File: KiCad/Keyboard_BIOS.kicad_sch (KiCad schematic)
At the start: 19 parts, among them J1 Keyboard, J2 Mouse, U4 8242KBD, U401 74F32, U5 SST39SF010A, U61 74LS06

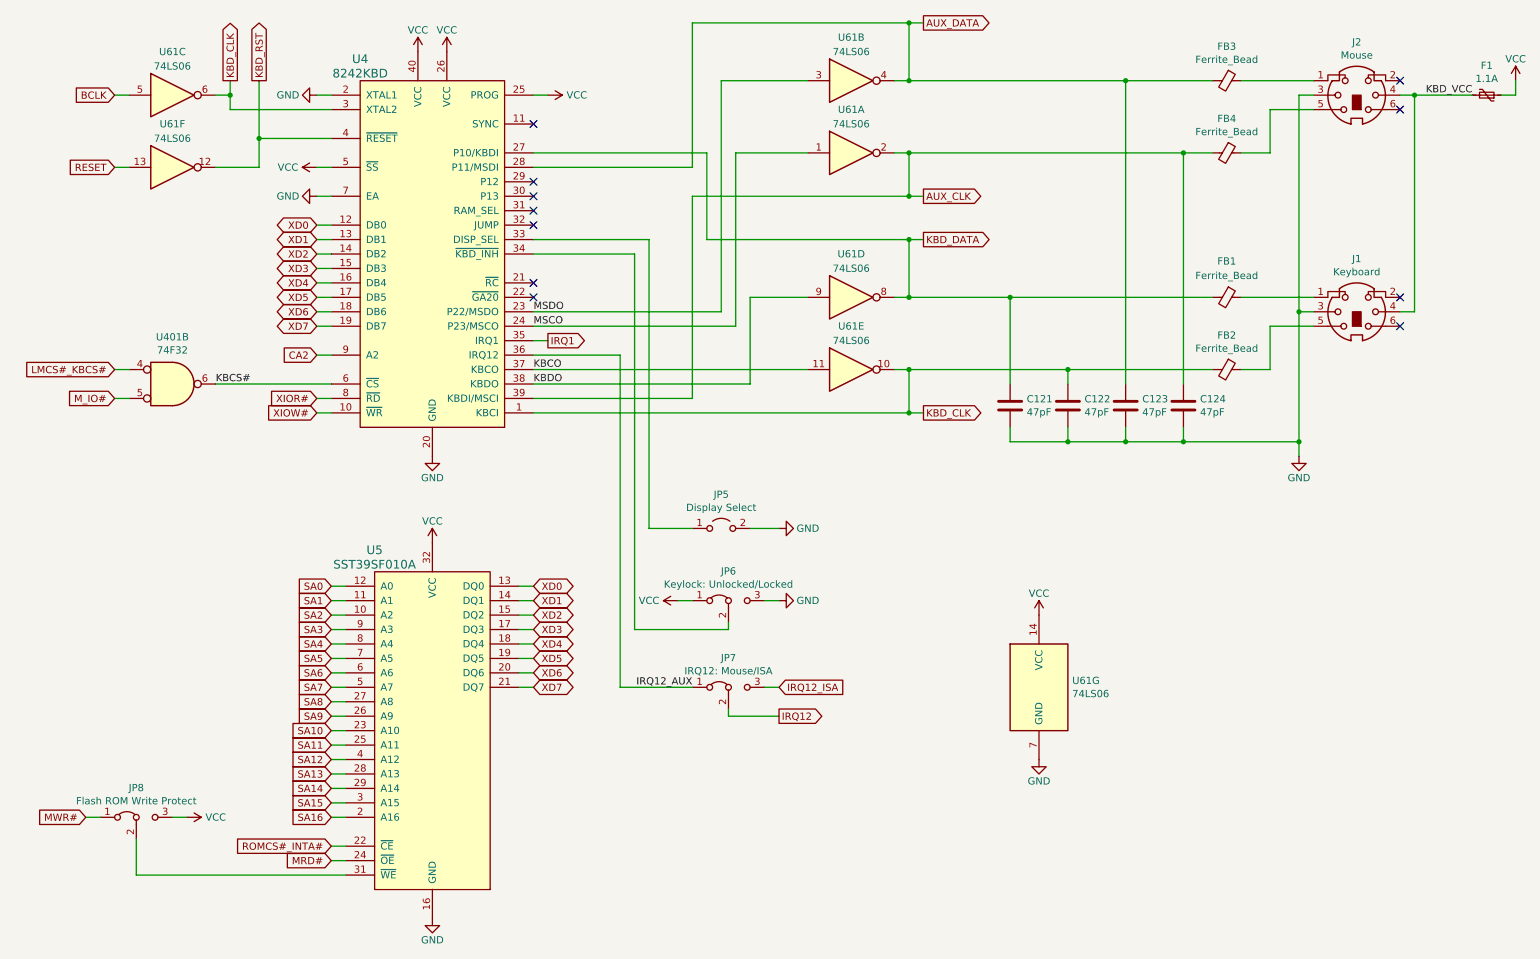
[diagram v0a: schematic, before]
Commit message: Version 0.3: Update DRAM schematic, pull-ups/pull-downs, CPU configuration jumpers
Signed-off-by: Sergey Kiselev <skiselev@gmail.com>
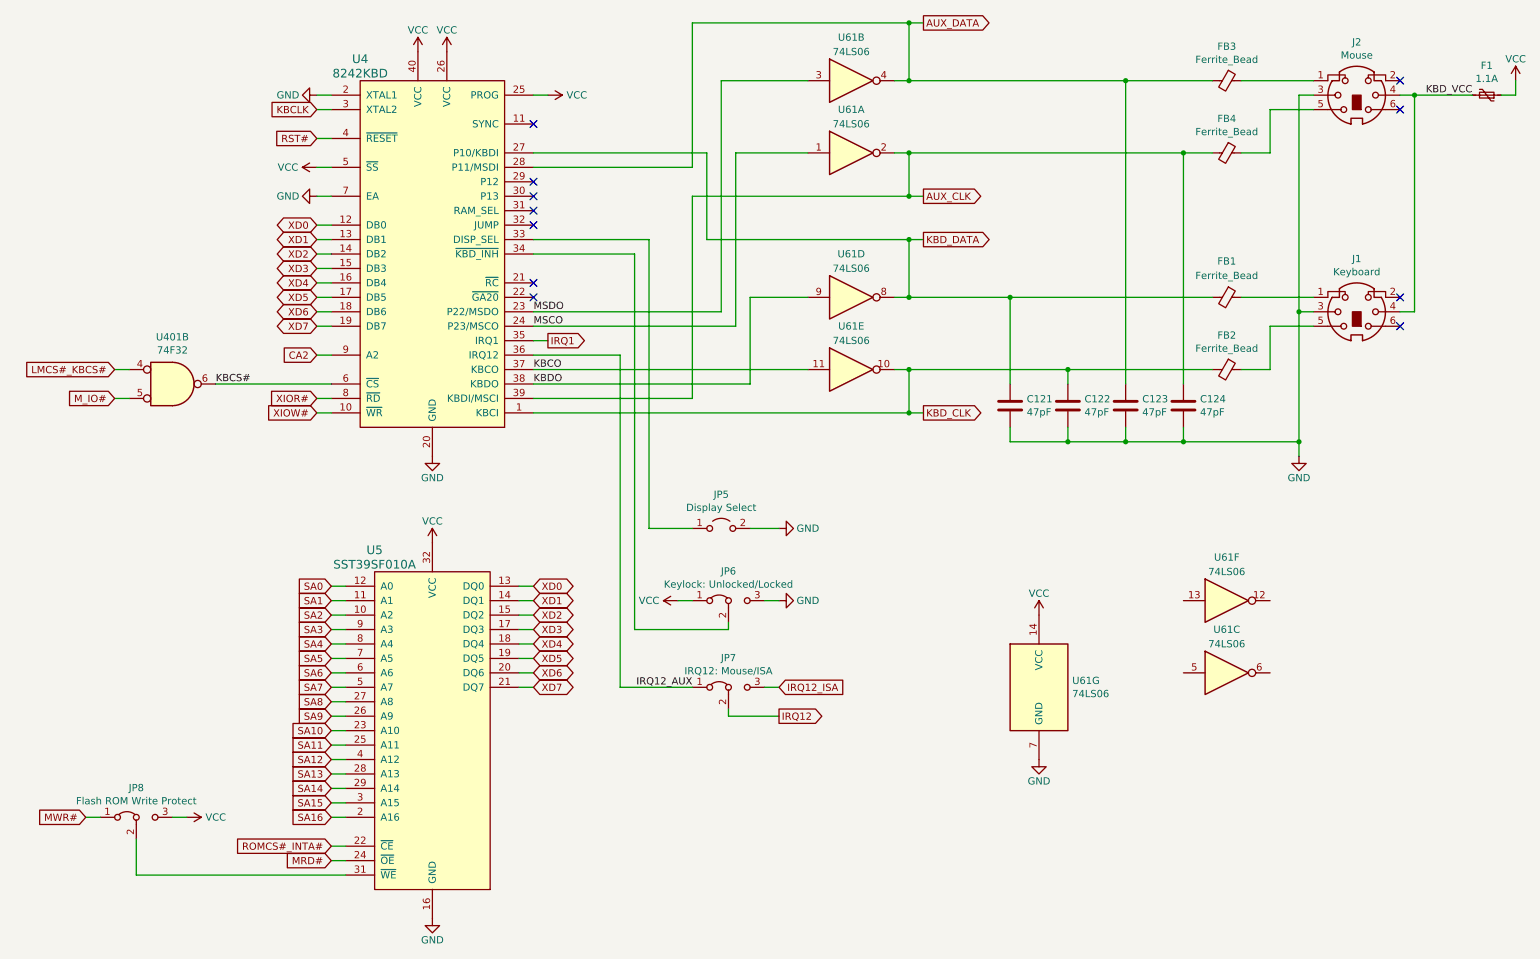
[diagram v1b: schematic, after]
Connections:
- net KBD_CLK: no longer U4.3 (XTAL2), U61.6
- net BCLK: no longer names the net of U61.5
- net KBD_RST: no longer names the net of U61.12
- net KBD_RST: no longer U4.4 (~{RESET})
- net RESET: no longer names the net of U61.13
- new net KBCLK: U4.3 (XTAL2)
- new net RST#: U4.4 (~{RESET})
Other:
- moved on the sheet: U61C, U61F
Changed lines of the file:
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@@
   (junction (at 215.9 48.26) (diameter 0) (color 0 0 0 0)
   )
-  (junction (at 48.26 38.1) (diameter 0) (color 0 0 0 0)
-  )
   (junction (at 256.54 38.1) (diameter 0) (color 0 0 0 0)
   )
@@
   )
   (junction (at 215.9 99.06) (diameter 0) (color 0 0 0 0)
-  )
-  (junction (at 53.34 45.72) (diameter 0) (color 0 0 0 0)
   )
   (junction (at 195.58 86.36) (diameter 0) (color 0 0 0 0)
@@
     (stroke (width 0) (type default) (color 0 0 0 0))
   )
-  (wire (pts (xy 48.26 38.1) (xy 48.26 40.64))
-    (stroke (width 0) (type default) (color 0 0 0 0))
-  )
   (wire (pts (xy 68.58 124.46) (xy 66.04 124.46))
     (stroke (width 0) (type default) (color 0 0 0 0))
@@
     (stroke (width 0) (type default) (color 0 0 0 0))
   )
-  (wire (pts (xy 45.72 38.1) (xy 48.26 38.1))
-    (stroke (width 0) (type default) (color 0 0 0 0))
-  )
   (wire (pts (xy 101.6 81.28) (xy 104.14 81.28))
     (stroke (width 0) (type default) (color 0 0 0 0))
@@
     (stroke (width 0) (type default) (color 0 0 0 0))
   )
-  (wire (pts (xy 53.34 45.72) (xy 53.34 35.56))
-    (stroke (width 0) (type default) (color 0 0 0 0))
-  )
   (wire (pts (xy 137.16 78.74) (xy 137.16 48.26))
     (stroke (width 0) (type default) (color 0 0 0 0))
@@
     (stroke (width 0) (type default) (color 0 0 0 0))
   )
-  (wire (pts (xy 48.26 40.64) (xy 66.04 40.64))
-    (stroke (width 0) (type default) (color 0 0 0 0))
-  )
   (wire (pts (xy 205.74 88.9) (xy 205.74 35.56))
     (stroke (width 0) (type default) (color 0 0 0 0))
   )
-  (wire (pts (xy 48.26 35.56) (xy 48.26 38.1))
-    (stroke (width 0) (type default) (color 0 0 0 0))
-  )
   (wire (pts (xy 238.76 38.1) (xy 236.22 38.1))
     (stroke (width 0) (type default) (color 0 0 0 0))
@@
     (stroke (width 0) (type default) (color 0 0 0 0))
   )
-  (wire (pts (xy 30.48 50.8) (xy 27.94 50.8))
-    (stroke (width 0) (type default) (color 0 0 0 0))
-  )
   (wire (pts (xy 116.84 142.24) (xy 129.54 142.24))
     (stroke (width 0) (type default) (color 0 0 0 0))
@@
     (stroke (width 0) (type default) (color 0 0 0 0))
   )
-  (wire (pts (xy 53.34 50.8) (xy 45.72 50.8))
-    (stroke (width 0) (type default) (color 0 0 0 0))
-  )
-  (wire (pts (xy 30.48 38.1) (xy 27.94 38.1))
+  (wire (pts (xy 66.04 40.64) (xy 63.5 40.64))
     (stroke (width 0) (type default) (color 0 0 0 0))
   )
@@
     (stroke (width 0) (type default) (color 0 0 0 0))
   )
-  (wire (pts (xy 66.04 45.72) (xy 53.34 45.72))
+  (wire (pts (xy 66.04 45.72) (xy 63.5 45.72))
     (stroke (width 0) (type default) (color 0 0 0 0))
   )
@@
   )
   (wire (pts (xy 220.98 73.66) (xy 185.42 73.66))
-    (stroke (width 0) (type default) (color 0 0 0 0))
-  )
-  (wire (pts (xy 53.34 45.72) (xy 53.34 50.8))
     (stroke (width 0) (type default) (color 0 0 0 0))
   )
@@
     )
   )
-  (global_label "RESET" (shape input) (at 27.94 50.8 180) (fields_autoplaced)
-    (effects (font (size 1.27 1.27)) (justify right))
-    (property "Intersheet References" "${INTERSHEET_REFS}" (id 0) (at 0 0 0)
-      (effects (font (size 1.27 1.27)) hide)
-    )
-  )
   (global_label "SA7" (shape input) (at 66.04 142.24 180) (fields_autoplaced)
     (effects (font (size 1.27 1.27)) (justify right))
@@
     )
   )
-  (global_label "KBD_RST" (shape output) (at 53.34 35.56 90) (fields_autoplaced)
-    (effects (font (size 1.27 1.27)) (justify left))
-    (property "Intersheet References" "${INTERSHEET_REFS}" (id 0) (at 0 0 0)
-      (effects (font (size 1.27 1.27)) hide)
-    )
-  )
   (global_label "XIOW#" (shape input) (at 63.5 93.98 180) (fields_autoplaced)
     (effects (font (size 1.27 1.27)) (justify right))
@@
     )
   )
-  (global_label "BCLK" (shape input) (at 27.94 38.1 180) (fields_autoplaced)
-    (effects (font (size 1.27 1.27)) (justify right))
-    (property "Intersheet References" "${INTERSHEET_REFS}" (id 0) (at 0 0 0)
-      (effects (font (size 1.27 1.27)) hide)
+  (global_label "KBCLK" (shape input) (at 63.5 40.64 180) (fields_autoplaced)
+    (effects (font (size 1.27 1.27)) (justify right))
+    (property "Intersheet References" "${INTERSHEET_REFS}" (id 0) (at 55.0677 40.5606 0)
+      (effects (font (size 1.27 1.27)) (justify right) hide)
     )
   )
@@
     )
   )
+  (global_label "RST#" (shape input) (at 63.5 45.72 180) (fields_autoplaced)
+    (effects (font (size 1.27 1.27)) (justify right))
+    (property "Intersheet References" "${INTERSHEET_REFS}" (id 0) (at 56.4587 45.7994 0)
+      (effects (font (size 1.27 1.27)) (justify right) hide)
+    )
+  )
   (global_label "SA9" (shape input) (at 66.04 147.32 180) (fields_autoplaced)
     (effects (font (size 1.27 1.27)) (justify right))
@@
   (global_label "SA12" (shape input) (at 66.04 154.94 180) (fields_autoplaced)
     (effects (font (size 1.27 1.27)) (justify right))
-    (property "Intersheet References" "${INTERSHEET_REFS}" (id 0) (at 0 0 0)
-      (effects (font (size 1.27 1.27)) hide)
-    )
-  )
-  (global_label "KBD_CLK" (shape output) (at 48.26 35.56 90) (fields_autoplaced)
-    (effects (font (size 1.27 1.27)) (justify left))
     (property "Intersheet References" "${INTERSHEET_REFS}" (id 0) (at 0 0 0)
       (effects (font (size 1.27 1.27)) hide)
@@
     (pin "4")
   )
-  (symbol (lib_id "74xx:74LS06") (at 38.1 38.1 0) (unit 3)
-    (in_bom yes) (on_board yes)
-    (property "Reference" "U61" (id 0) (at 38.1 30.48 0))
-    (property "Value" "74LS06" (id 1) (at 38.1 33.02 0))
-    (property "Footprint" "" (id 2) (at 38.1 38.1 0)
-      (effects (font (size 1.27 1.27)) hide)
-    )
-    (property "Datasheet" "http://www.ti.com/lit/gpn/sn74LS06" (id 3) (at 38.1 38.1 0)
+  (symbol (lib_id "74xx:74LS06") (at 223.52 139.7 0) (unit 3)
+    (in_bom yes) (on_board yes)
+    (property "Reference" "U61" (id 0) (at 223.52 132.08 0))
+    (property "Value" "74LS06" (id 1) (at 223.52 134.62 0))
+    (property "Footprint" "" (id 2) (at 223.52 139.7 0)
+      (effects (font (size 1.27 1.27)) hide)
+    )
+    (property "Datasheet" "http://www.ti.com/lit/gpn/sn74LS06" (id 3) (at 223.52 139.7 0)
       (effects (font (size 1.27 1.27)) hide)
     )
@@
     (pin "11")
   )
-  (symbol (lib_id "74xx:74LS06") (at 38.1 50.8 0) (unit 6)
-    (in_bom yes) (on_board yes)
-    (property "Reference" "U61" (id 0) (at 38.1 43.18 0))
-    (property "Value" "74LS06" (id 1) (at 38.1 45.72 0))
-    (property "Footprint" "" (id 2) (at 38.1 50.8 0)
-      (effects (font (size 1.27 1.27)) hide)
-    )
-    (property "Datasheet" "http://www.ti.com/lit/gpn/sn74LS06" (id 3) (at 38.1 50.8 0)
-      (effects (font (size 1.27 1.27)) hide)
-    )
+  (symbol (lib_id "74xx:74LS06") (at 223.52 127 0) (unit 6)
+    (in_bom yes) (on_board yes)
+    (property "Reference" "U61" (id 0) (at 223.52 119.38 0))
+    (property "Value" "74LS06" (id 1) (at 223.52 121.92 0))
+    (property "Footprint" "" (id 2) (at 223.52 127 0)
+      (effects (font (size 1.27 1.27)) hide)
+    )
+    (property "Datasheet" "http://www.ti.com/lit/gpn/sn74LS06" (id 3) (at 223.52 127 0)
+      (effects (font (size 1.27 1.27)) hide)
+    )

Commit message: Version 0.4: Update chipset connection
Signed-off-by: Sergey Kiselev <skiselev@gmail.com>
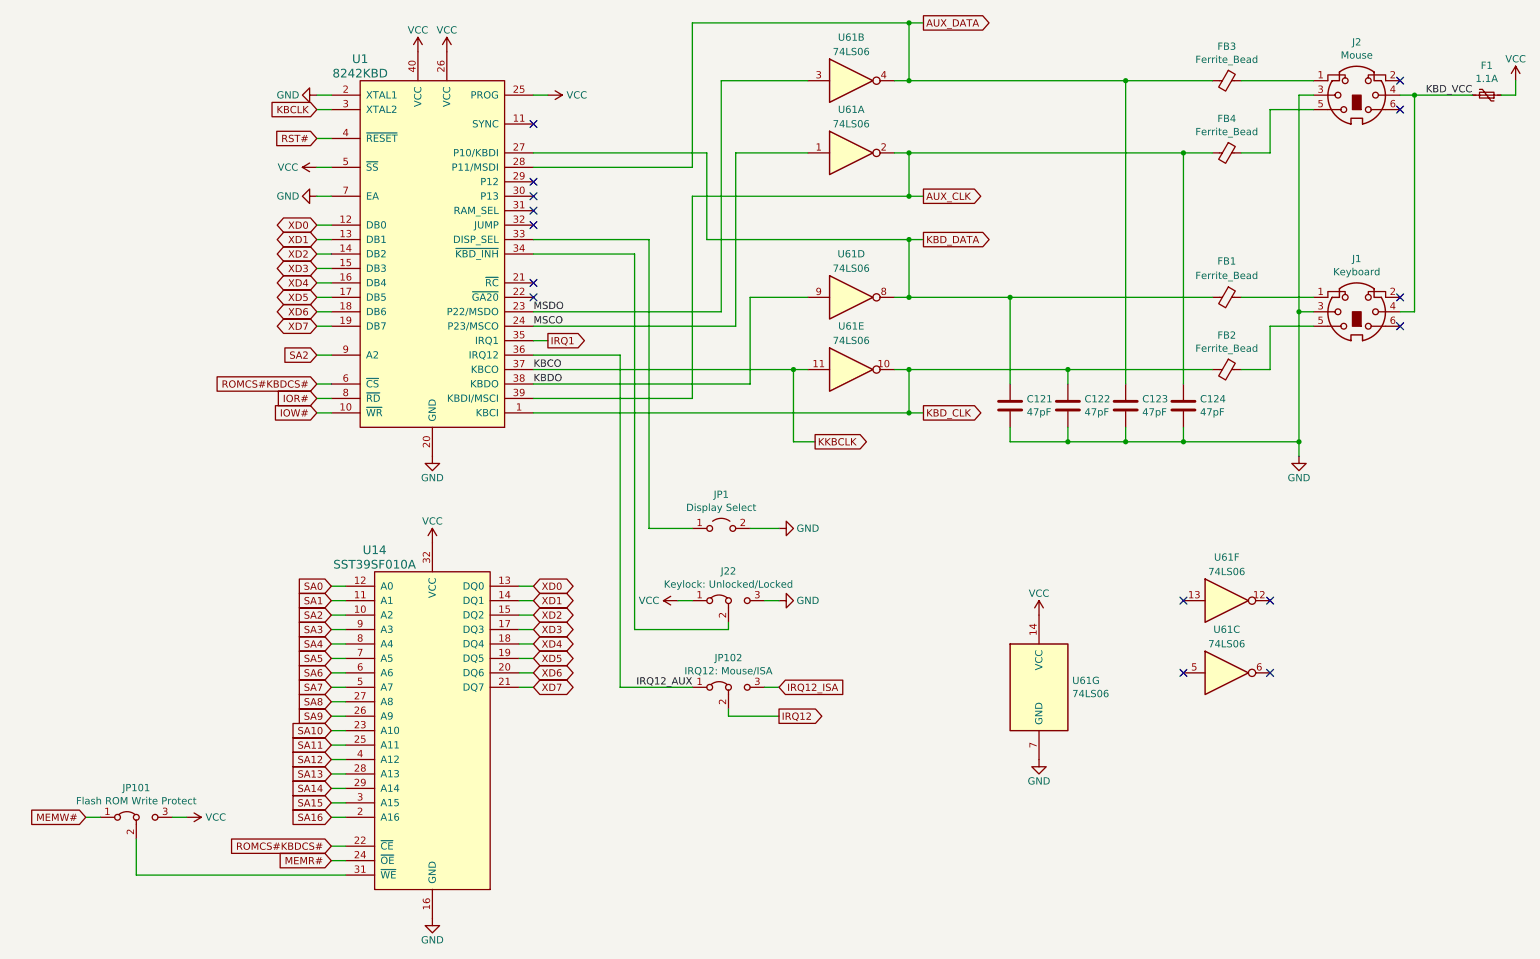
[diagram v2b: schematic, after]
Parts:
- removed U401: 74F32, symbol 74xx:74LS32
- C121, C122, C123, C124: footprint (none) -> Capacitor_SMD:C_0603_1608Metric_Pad1.08x0.95mm_HandSolder
- F1: footprint (none) -> Fuse:Fuse_Littelfuse_395Series
- FB1, FB2, FB3, FB4: footprint (none) -> Inductor_SMD:L_0603_1608Metric_Pad1.05x0.95mm_HandSolder; symbol Device:Ferrite_Bead_Small -> Device:FerriteBead_Small
- J1, J2: footprint (none) -> My_Components:Conn_Mini_DIN_6pin
- J22: renamed from JP6; footprint (none) -> My_Components:Conn_Pin_Header_3x1_2.54mm
- JP1: renamed from JP5; footprint (none) -> My_Components:Conn_Pin_Header_2x1_2.54mm
- JP101: renamed from JP8; footprint (none) -> My_Components:Conn_Pin_Header_3x1_2.54mm
- JP102: renamed from JP7; footprint (none) -> My_Components:Conn_Pin_Header_3x1_2.54mm
- U1: renamed from U4; footprint *DIP*40* -> My_Components:IC_DIP40_600
- U14: renamed from U5; footprint (none) -> My_Components:IC_DIP32_600
- U61: footprint (none) -> My_Components:IC_DIP14_300
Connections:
- net CA2 is gone; now on net SA2: U1.9 (A2)
- net ROMCS#_INTA# is gone; now on net ROMCS#KBDCS#: U14.22 (~{CE})
- net KBCO renamed KKBCLK
- net KBCS# renamed ROMCS#KBDCS#
- net MRD# renamed MEMR#
- net MWR# renamed MEMW#
- net XIOR# renamed IOR#
- net XIOW# renamed IOW#
- no-connect marks 11 -> 15
